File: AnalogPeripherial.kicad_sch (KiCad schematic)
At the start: 24 parts, among them J1 SD_Card_Receptacle, U1 74HC7014, U2 LD1117S33TR_SOT223, U3 STM32F407VGTx, U4 TLV9061xDBV

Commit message: Almost finished schemat design
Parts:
- removed U3: STM32F407VGTx, Package_QFP:LQFP-100_14x14mm_P0.5mm, symbol MCU_ST_STM32F4:STM32F407VGTx
- added C10, C11, C12, C13, C9: 100n, symbol Device:C
- added C14, C15, C16, C17, C18, C19: C, symbol Device:C
- added D1: LED, symbol Device:LED
- added J2: USB_B_Mini, symbol Connector:USB_B_Mini
- added J3: USART, symbol Connector:Conn_01x04_Pin
- added R10, R11: 1.5k, symbol Device:R
- added R12: R, symbol Device:R
- added SW1: record, symbol Switch:SW_Push
- added SW2: replay, symbol Switch:SW_Push
- added U3: LM386, symbol Amplifier_Audio:LM386
- added U5: STM32F373CCTx, Package_QFP:LQFP-48_7x7mm_P0.5mm, symbol MCU_ST_STM32F3:STM32F373CCTx
- added Y1: Crystal, symbol Device:Crystal
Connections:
- net 3V3: now also C10.1, C11.1, C12.1, C9.1, D1.2 (A), J3.1 (Pin_1), R10.1
- net GND: now also LS1.2, C13.2, C14.2, C15.2, C19.1, J2.5 (GND), J3.4 (Pin_4), R11.2, R12.2, SW1.2, SW2.2, U3.4 (GND), U5.23 (VSSSD), U5.47 (VSS), U5.8 (VSSA)
- net MISO: now also U5.40 (PB4)
- net MOSI: now also U5.41 (PB5)
- net at LS1.1: now also C17.2
- net VCC renamed VBUS
- net VBUS: now also J2.1 (VBUS), U3.6 (V+)
- new net: C16.2, R12.1
- new net: C18.1, U3.1 (GAIN)
- new net: C18.2, U3.8 (GAIN)
- new net: C16.1, C17.1, U3.5
- new net: C19.2, U3.7 (BYPASS)
- new net: C10.2, C11.2, C12.2, C9.2, U5.1 (VBAT), U5.17 (VDD), U5.24 (VDDSD), U5.48 (VDD), U5.9 (VDDA)
- new net: D1.1 (K), R11.1
- new net BOOT0: U5.44 (BOOT0)
- new net DAC: U3.3 (+), U5.14 (PA4)
- new net HSE_IN: C14.1, U5.5 (PF0), Y1.1
- new net HSE_OUT: C15.1, U5.6 (PF1), Y1.2
- new net NRST: C13.1, U5.7 (NRST)
- new net USART_RX: J3.3 (Pin_3), U5.31 (PA10)
- new net USART_TX: J3.2 (Pin_2), U5.30 (PA9)
- new net USB+: J2.3 (D+), R10.2, U5.33 (PA12)
- new net USB-: J2.2 (D-), U5.32 (PA11)
- new net record: SW1.1
- new net replay: SW2.1
- no-connect marks 86 -> 4
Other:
- note removed: "0. Zdecydować który mikrofon 1. Zdecydować się czy na pewno takie schemat (poczytać bardziej) 2. Wyliczyć wartość (jestem bardziej za tym który tutaj jest bo ten wzmacniacz jest w tme ;) Materiały są na overflow lub w tym katalogu"
- note removed: "ADC"
- note removed: "Battery"
- note removed: "USB"
- moved on the sheet: C2, C3, LS1, U2

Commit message: Almost finish schematic
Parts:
- removed C4: C, symbol Device:C
- added C10: 0.1u, symbol Device:C
- added C11: 10u, symbol Device:C
- added C8, C9: 100n, symbol Device:C
- added FB1: FerriteBead, symbol Device:FerriteBead
- added RV1: 10k, symbol Device:R_Potentiometer
- C1: renamed from C12; value 100n -> 10u
- C12: renamed from C18; value C -> 10u
- C13: renamed from C19; value C -> 100p
- C14: renamed from C16; value C -> 0.047u
- C15: renamed from C5; value C -> 330n
- C17: value C -> 470u
- C18: renamed from C7; value C -> 47u
- C20: renamed from C6; value C -> 120p
- C21: renamed from C8; value C -> 3.3u
- R2: renamed from R4; value R -> 5.9k
- R3: renamed from R12; value R -> 10
- R4: renamed from R5; value R -> 200k
- R5: renamed from R6; value R -> 200k
- R6: renamed from R8; value R -> 787
- R7, R9: value R -> 10k
- Y1: footprint (none) -> Crystal:Crystal_HC18-U_Vertical
- renumbered C2 to C16, C3 to C19, C13 to C2, C1 to C22, C14 to C3, C11 to C4, C15 to C5, C10 to C6, C9 to C7, J3 to J1, J1 to J3, R10 to R1, R1 to R10, R2 to R11, R3 to R12, R11 to R8, U5 to U1, U3 to U2, U2 to U3, U1 to U5
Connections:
- net CS: now also U1.14 (PA4)
- net DAC: now also U1.15 (PA5), RV1.1; no longer U1.14 (PA4), U2.3 (+)
- net GND: now also R9.1, U2.2 (-), RV1.3; no longer C21.1
- net record: now also U1.18 (PB0)
- net replay: now also U1.19 (PB1)
- net at C20.2, R7.2, U4.1: now also C21.1; no longer R9.1
- net at C1.2, C4.2, C6.2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: no longer U1.24 (VDDSD), U1.9 (VDDA)
- new net: C10.2, C11.2, C8.2, C9.2, FB1.2, U1.24 (VDDSD), U1.9 (VDDA)
- new net: RV1.2, U2.3 (+)
- new net 3VA3: C10.1, C11.1, C8.1, C9.1, FB1.1
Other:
- note removed: "MOSI czy dodać?"
- note removed: "sprawdzic piny"
- company: (none) -> Joanna Chrobot
- title: (none) -> Voice recording and playback system with STM32
- moved on the sheet: C1, C12, C13, C14, C15, C16, C17, C18, C19, C2, C20, C21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

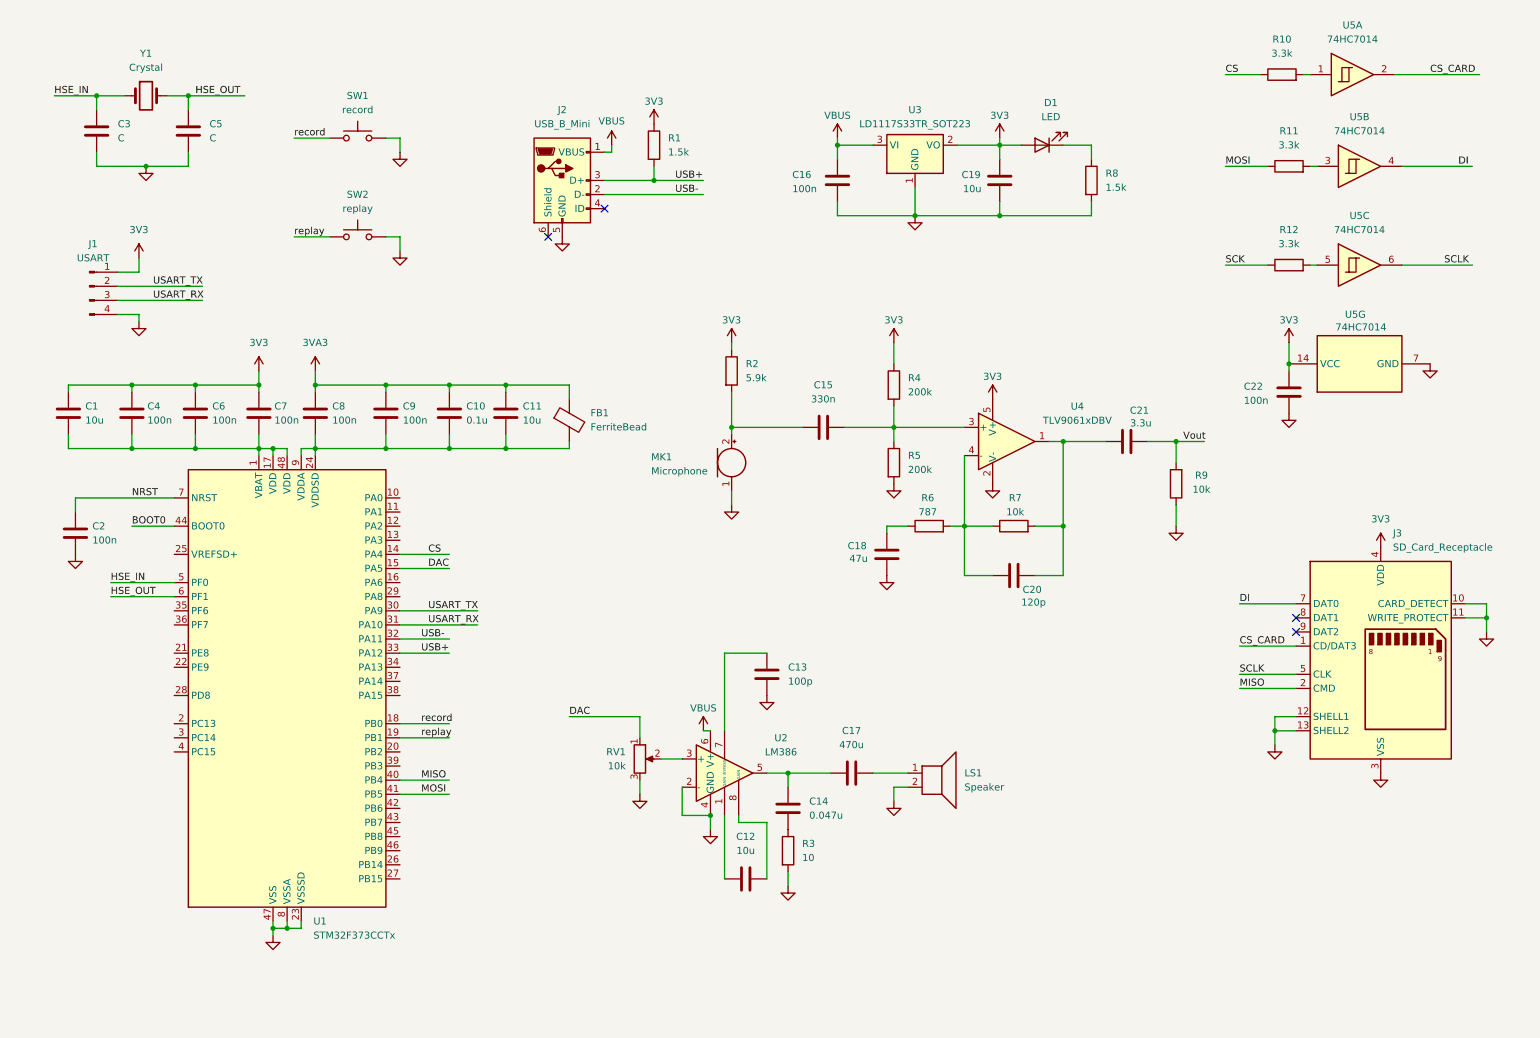
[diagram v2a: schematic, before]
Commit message: Removing buffor and add some new peripherials to stm32
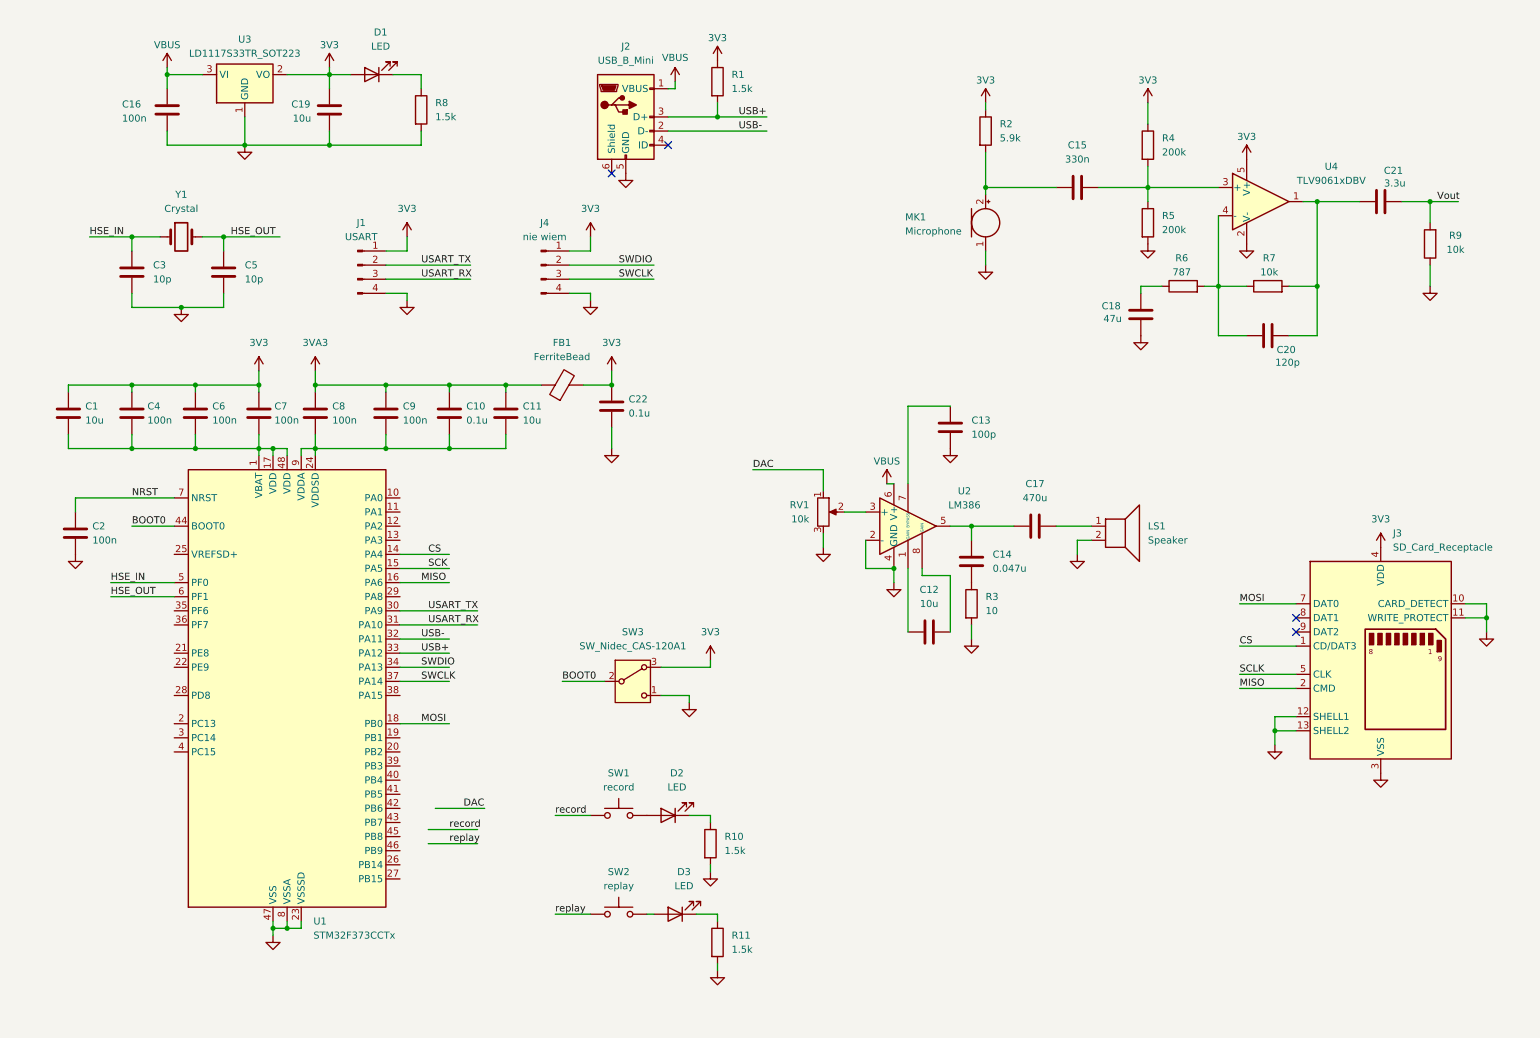
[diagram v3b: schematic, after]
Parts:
- removed R12: 3.3k, symbol Device:R
- removed U5: 74HC7014, Package_SO:SOIC-14_3.9x8.7mm_P1.27mm, symbol 74xx:74HC7014
- added D2, D3: LED, LED_SMD:LED_0805_2012Metric_Pad1.15x1.40mm_HandSolder, symbol Device:LED
- added J4: nie wiem, symbol Connector:Conn_01x04_Pin
- added SW3: SW_Nidec_CAS-120A1, Button_Switch_SMD:Nidec_Copal_CAS-120A, symbol Switch:SW_Nidec_CAS-120A1
- C1, C10, C11, C12, C13, C14, C15, C16, C17, C18, C19, C2, C20, C21, C4, C6, C7, C8, C9: footprint (none) -> Capacitor_SMD:C_0805_2012Metric_Pad1.18x1.45mm_HandSolder
- C22: value 100n -> 0.1u; footprint (none) -> Capacitor_SMD:C_0805_2012Metric_Pad1.18x1.45mm_HandSolder
- C3, C5: value C -> 10p; footprint (none) -> Capacitor_SMD:C_0805_2012Metric_Pad1.18x1.45mm_HandSolder
- D1: footprint (none) -> LED_SMD:LED_0805_2012Metric_Pad1.15x1.40mm_HandSolder
- FB1: footprint (none) -> Inductor_SMD:L_0805_2012Metric_Pad1.05x1.20mm_HandSolder
- J1: footprint (none) -> Connector_PinHeader_2.54mm:PinHeader_1x04_P2.54mm_Vertical
- J2: footprint (none) -> Connector_USB:USB_Mini-B_Lumberg_2486_01_Horizontal
- R1, R2, R3, R4, R5, R6, R7, R8, R9: footprint (none) -> Resistor_SMD:R_0805_2012Metric_Pad1.20x1.40mm_HandSolder
- R10, R11: value 3.3k -> 1.5k; footprint (none) -> Resistor_SMD:R_0805_2012Metric_Pad1.20x1.40mm_HandSolder
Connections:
- net CS_CARD is gone; now on net CS: J3.1 (CD/DAT3)
- net DI is gone; now on net MOSI: J3.7 (DAT0)
- net 3V3: now also FB1.2, J4.1 (Pin_1), SW3.3 (A)
- net BOOT0: now also SW3.2 (B)
- net CS: no longer R10.1
- net DAC: no longer U1.15 (PA5)
- net GND: now also R10.2, R11.2, J4.4 (Pin_4), SW3.1 (C); no longer SW1.2, SW2.2
- net MISO: now also U1.16 (PA6); no longer U1.40 (PB4)
- net MOSI: now also U1.18 (PB0); no longer R11.1, U1.41 (PB5)
- net SCK: now also U1.15 (PA5)
- net record: no longer U1.18 (PB0)
- net replay: no longer U1.19 (PB1)
- net at C10.2, C11.2, C8.2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: no longer FB1.2
- net SWDIO: now reaches U1.34 (PA13)
- net SWDIO: now also J4.2 (Pin_2)
- net SWCLK: now reaches U1.37 (PA14)
- net SWCLK: now also J4.3 (Pin_3)
- new net: D3.1 (K), R11.1
- new net: D3.2 (A), SW2.2
- new net: D2.2 (A), SW1.2
- new net: D2.1 (K), R10.1
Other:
- moved on the sheet: C12, C13, C14, C15, C16, C17, C18, C19, C20, C21, C3, C5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

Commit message: Symulation microphone update, also peripherail correction with cubeIDE
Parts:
- J4: value nie wiem -> SWD
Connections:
- net SCLK is gone; now on net SPI1_SCK: J3.5 (CLK)
- net record is gone; now on net PUSH_REC: SW1.1
- net replay is gone; now on net PUSH_REPLAY: SW2.1
- net ADC1_IN1: now reaches U1.10 (PA0)
- net PUSH_REC: now reaches U1.19 (PB1)
- net PUSH_REPLAY: now reaches U1.20 (PB2)
- net SPI1_NSS: now reaches U1.38 (PA15)
- net SPI1_NSS: now also J3.1 (CD/DAT3)
- net CS renamed DAC1_OUT1
- net DAC1_OUT1: no longer J3.1 (CD/DAT3)
- net MISO renamed SPI1_MISO
- net MOSI renamed SPI1_MOSI
- net SCK renamed SPI1_SCK
- net Vout renamed ADC
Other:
- moved on the sheet: C2

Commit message: New footprint design: microphone, speaker and push button
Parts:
- J4: footprint (none) -> Connector_PinHeader_2.54mm:PinHeader_1x04_P2.54mm_Horizontal
- LS1: footprint (none) -> my_custom_stuff:speaker
- MK1: footprint (none) -> my_custom_stuff:microphone
- SW1, SW2: footprint (none) -> my_custom_stuff:button
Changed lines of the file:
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@@
 			)
 		)
-		(property "Footprint" ""
+		(property "Footprint" "my_custom_stuff:microphone"
 			(at 185.42 49.53 90)
 			(effects
@@
 			)
 		)
-		(property "Footprint" ""
+		(property "Footprint" "my_custom_stuff:button"
 			(at 119.38 153.67 0)
 			(effects
@@
 			)
 		)
-		(property "Footprint" ""
+		(property "Footprint" "my_custom_stuff:speaker"
 			(at 209.55 111.76 0)
 			(effects
@@
 			)
 		)
-		(property "Footprint" ""
+		(property "Footprint" "Connector_PinHeader_2.54mm:PinHeader_1x04_P2.54mm_Horizontal"
 			(at 105.41 59.69 0)
 			(effects
@@
 			)
 		)
-		(property "Footprint" ""
+		(property "Footprint" "my_custom_stuff:button"
 			(at 119.38 171.45 0)
 			(effects

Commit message: First stage of PCB design
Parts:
- removed J3: SD_Card_Receptacle, symbol Connector:SD_Card_Receptacle
- added U4: 112J-TDAR-R01, 112J_TDAR_R01:112J-TDAR-R01_ATT, symbol 2025-12-27_23-38-34:112J-TDAR-R01
- J2: renamed from J4; footprint Connector_PinHeader_2.54mm:PinHeader_1x04_P2.54mm_Horizontal -> Connector_PinHeader_2.54mm:PinHeader_1x04_P2.54mm_Vertical
- RV1: footprint (none) -> my_custom_stuff:potencjometr
- U3: renamed from U2; footprint (none) -> ADL5370ACPZ:M08A_TEX
- renumbered C2 to C1, C8 to C10, C9 to C11, C10 to C12, C11 to C13, C22 to C14, C12 to C15, C13 to C16, C14 to C17, C17 to C18, C15 to C19, C1 to C2, C18 to C20, C20 to C21, C21 to C22, C16 to C4, C4 to C5, C5 to C6, C6 to C7, C7 to C8, C19 to C9, J2 to J3, R8 to R1, R7 to R10, R9 to R11, R1 to R2, R10 to R3, R11 to R4, R3 to R5, R2 to R6, R4 to R7, R5 to R8, R6 to R9, U3 to U1, U1 to U2, U4 to U5
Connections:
- net ADC is gone; now on net ADC1_IN1: C22.2, R11.2
- net DAC is gone; now on net DAC1_OUT1: RV1.1
- net 3V3: now also U4.4
- net GND: now also C10.2, C11.2, C12.2, C13.2, C2.2, C5.2, C7.2, C8.2, U2.1 (VBAT), U2.17 (VDD), U2.24 (VDDSD), U2.48 (VDD), U2.9 (VDDA), U4.3
- net SPI1_MISO: now also U4.2
- net SPI1_MOSI: now also U4.7
- net SPI1_NSS: now also U4.1
- net SPI1_SCK: now also U4.5
- no-connect marks 4 -> 27
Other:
- note added: "Microcontoler pheripherials"
- note added: "Microphone"
- note added: "Power supply"
- note added: "SD card"
- note added: "Speaker"
- moved on the sheet: C1, C10, C11, C12, C13, C14, C15, C16, C17, C18, C19, C2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

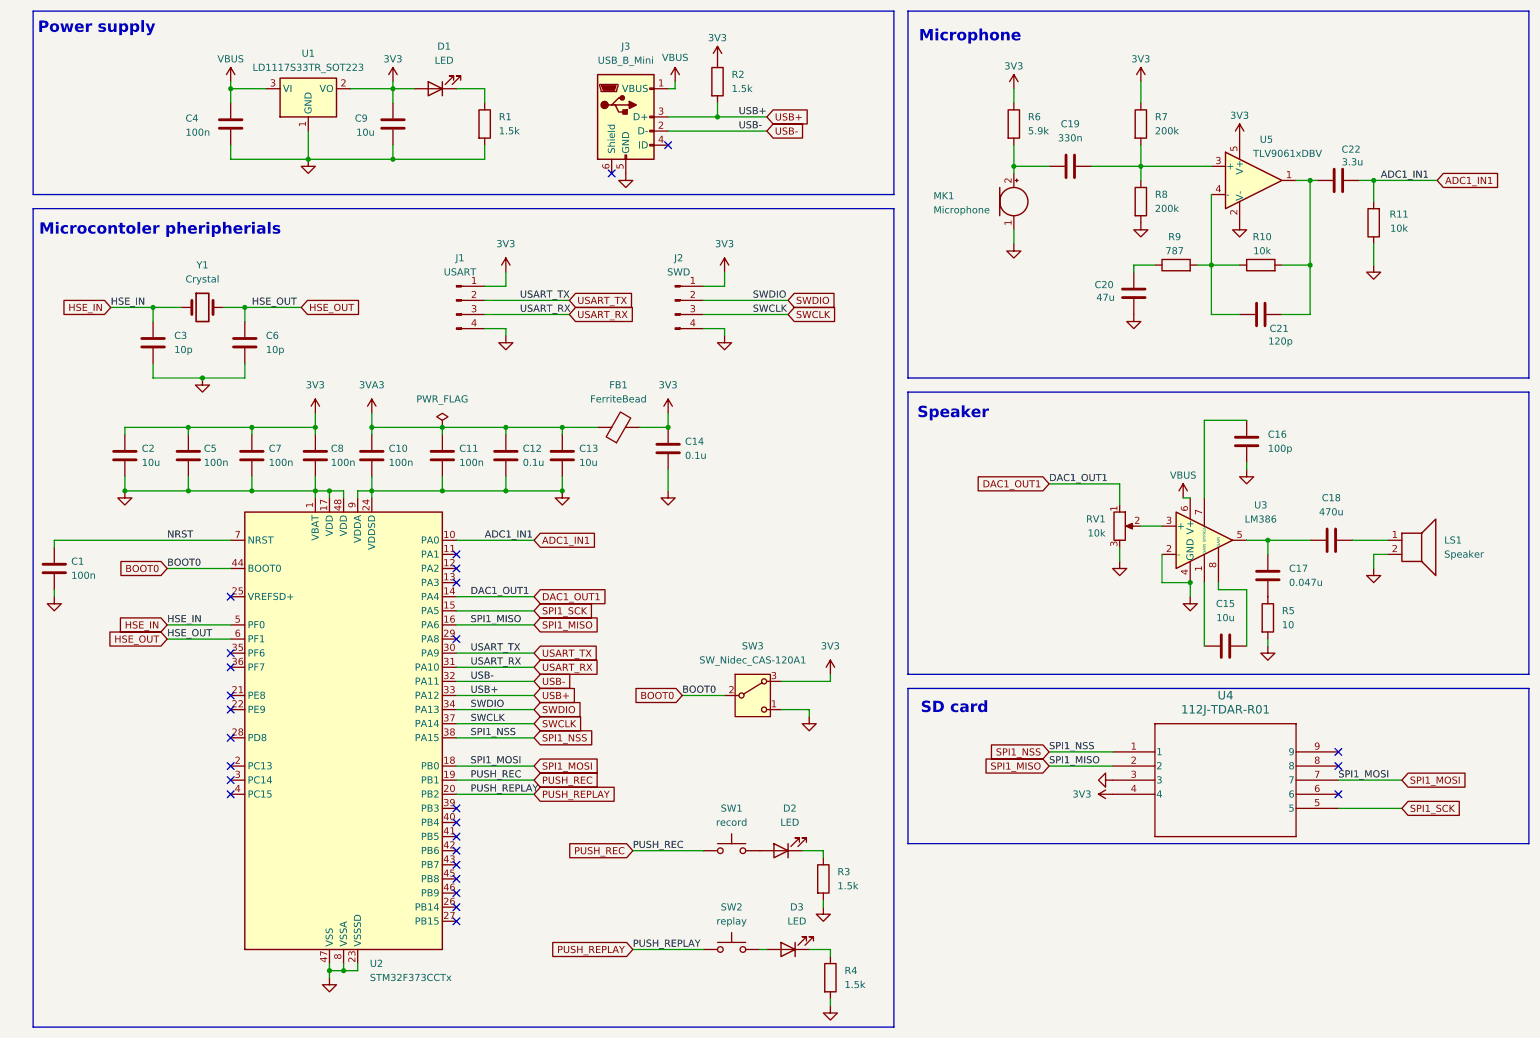
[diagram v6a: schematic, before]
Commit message: Add all footprint To do: 1. Add footprint and symbol to SD Card 2. Correct footprints and symobols 3. Finish the PCB design
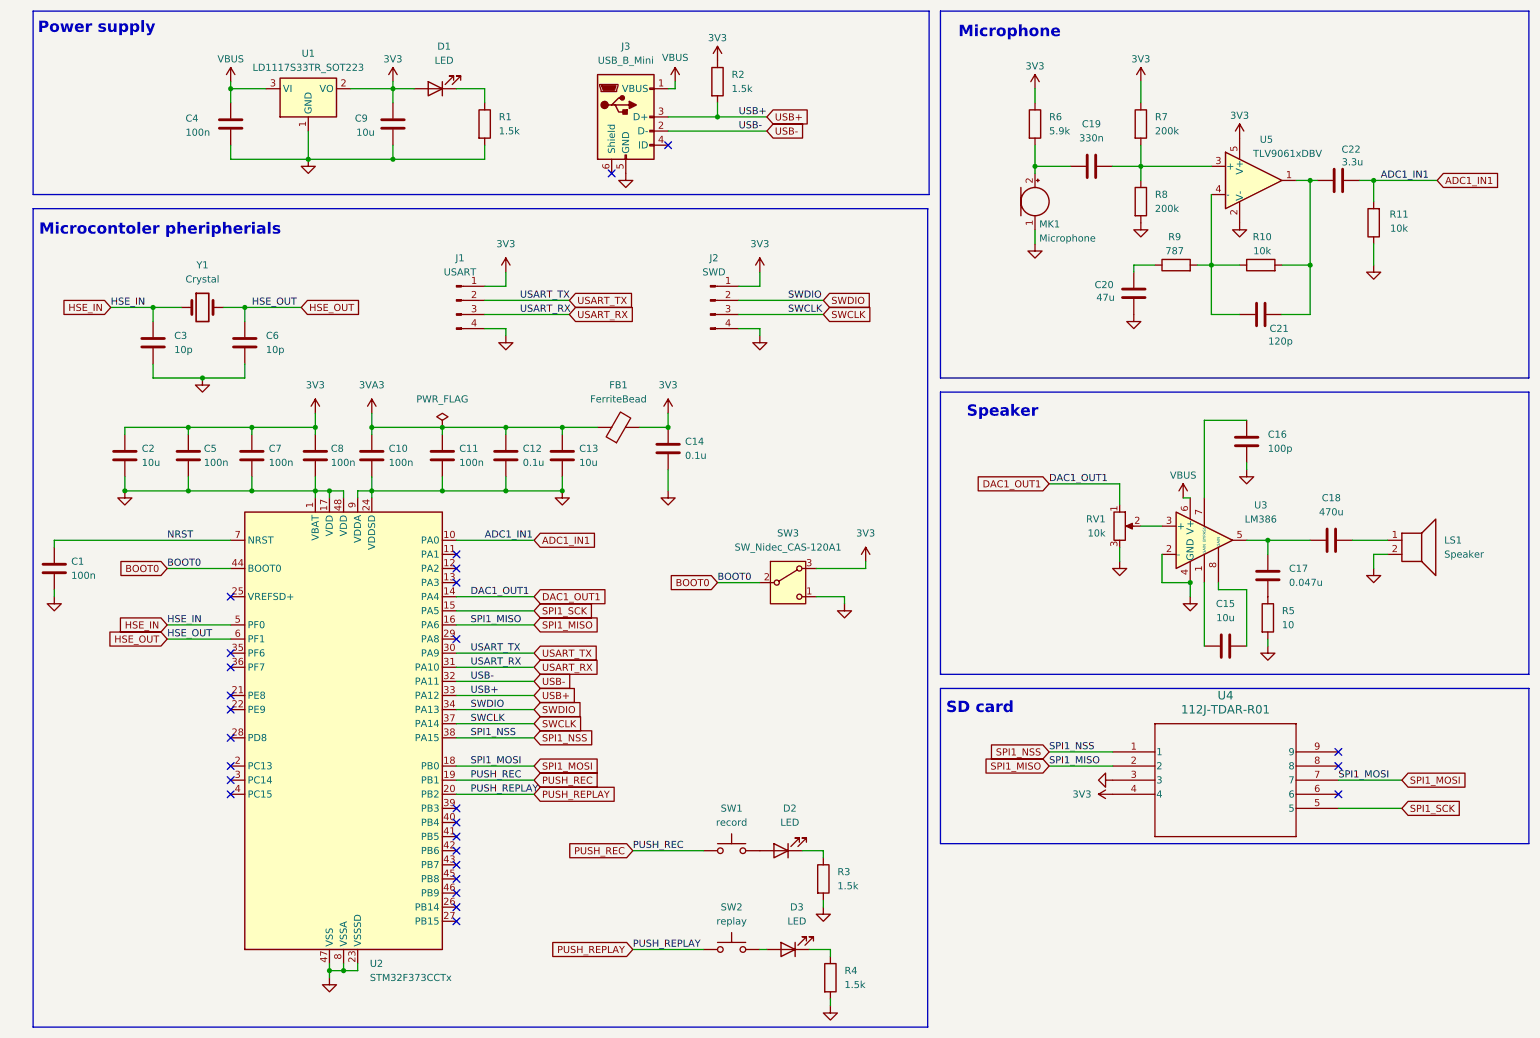
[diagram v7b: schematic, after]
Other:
- moved on the sheet: C19, J2, MK1, R6, SW3
